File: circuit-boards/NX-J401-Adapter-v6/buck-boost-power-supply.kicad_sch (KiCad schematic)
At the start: 55 parts, among them Q3 CSD19534Q5A, Q4 CSD17578Q5A, Q6 CSD19534Q5A, Q7 CSD17578Q5A

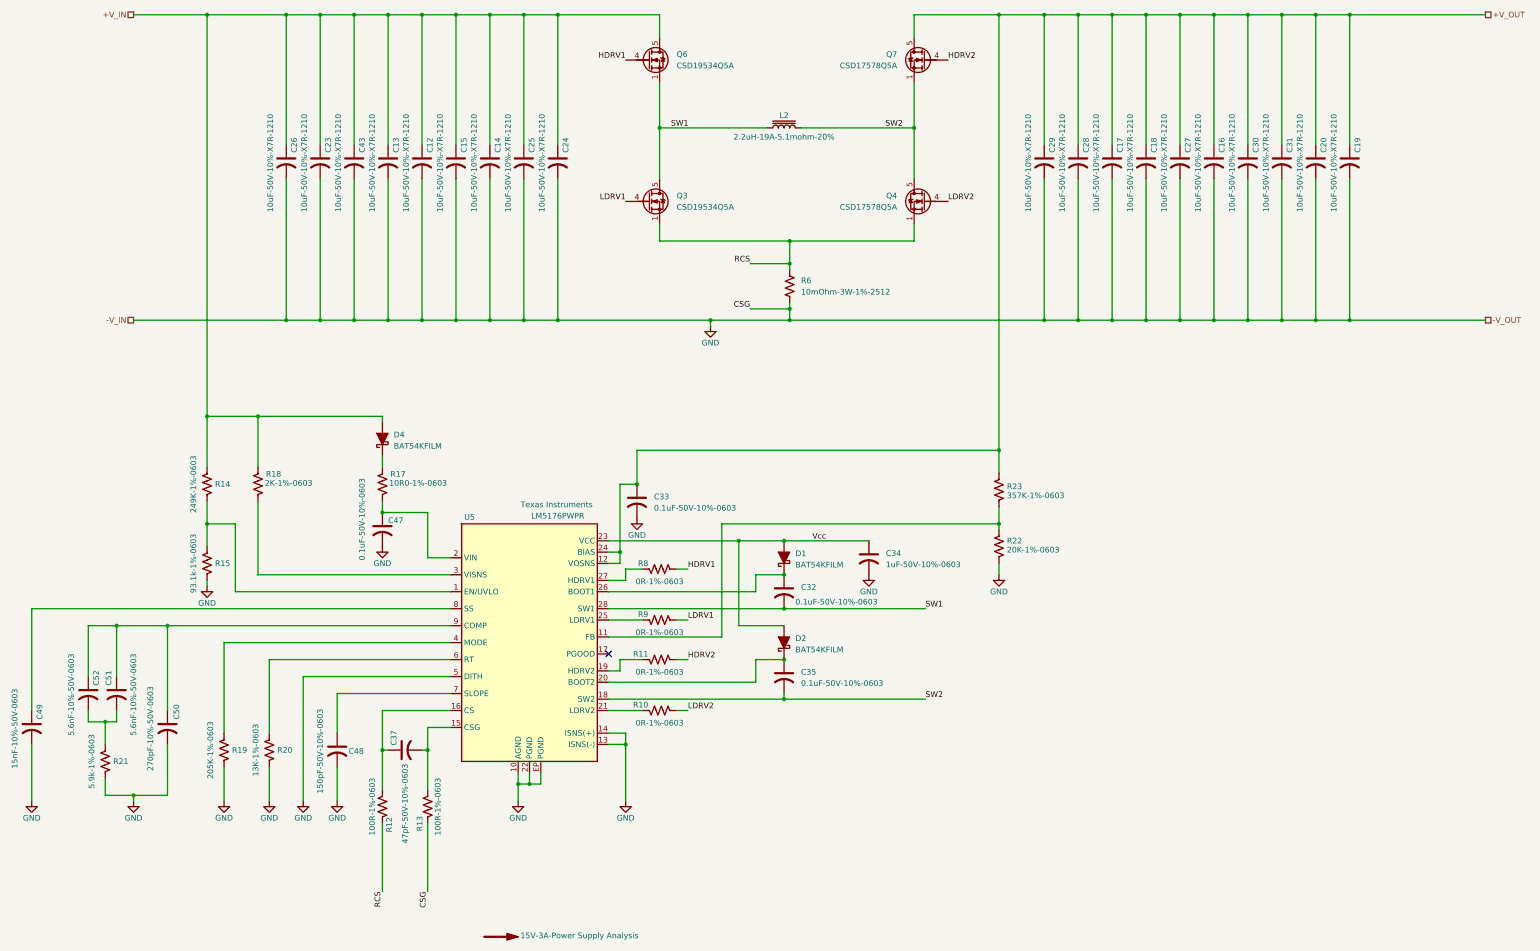
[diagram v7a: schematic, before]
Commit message: Adjusted connector positioning to more closely match J401.
Signed-off-by: Scott Berman <sgberman1@gmail.com>
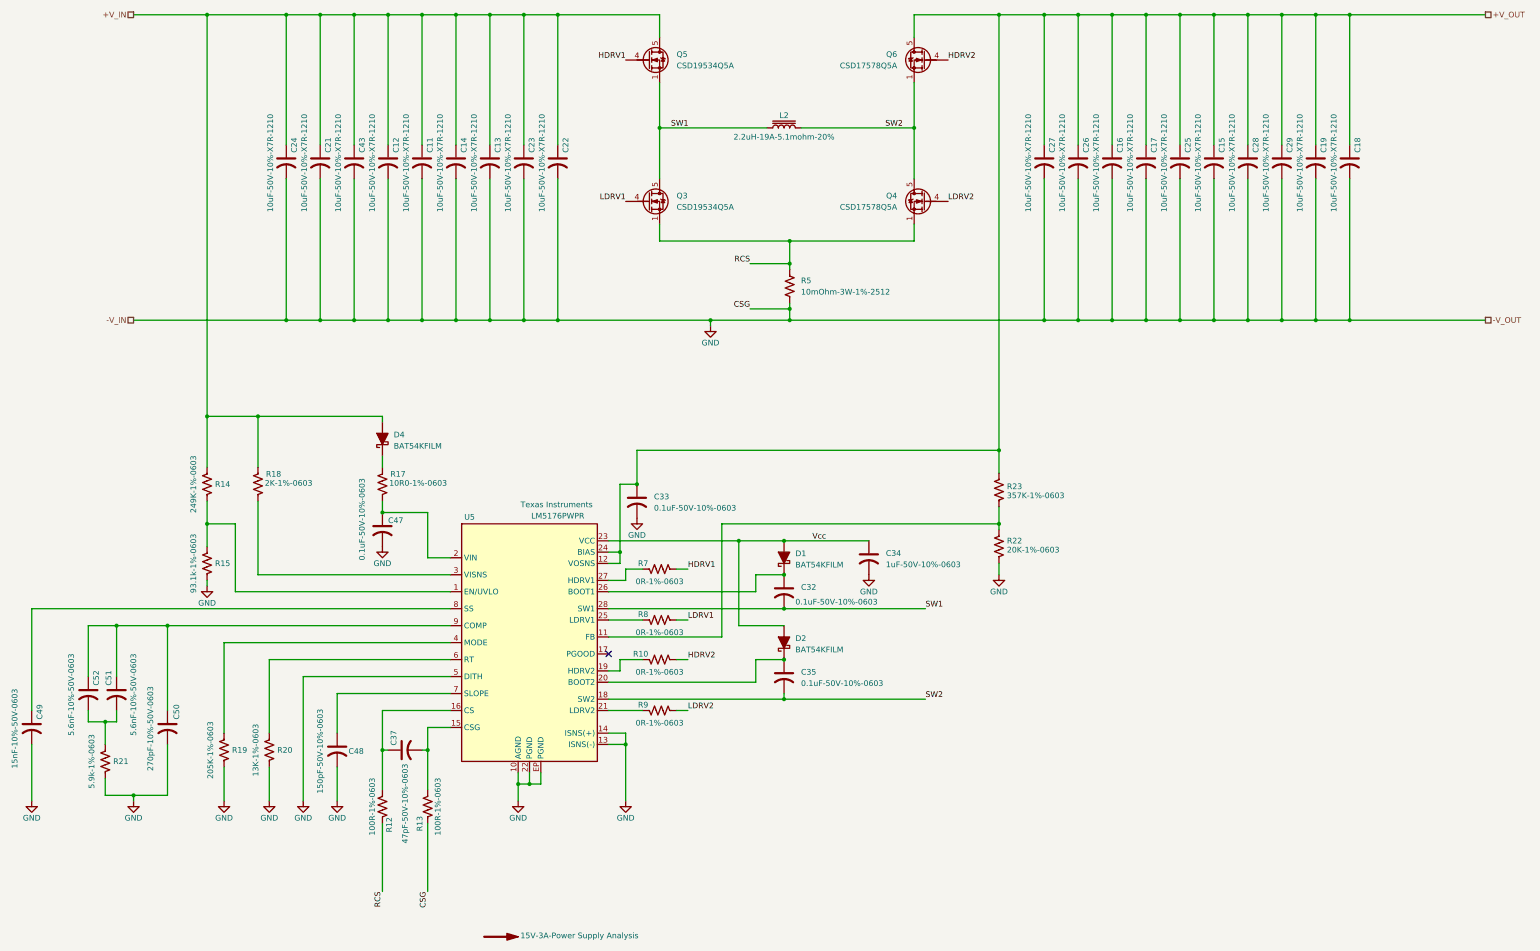
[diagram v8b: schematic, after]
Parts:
- renumbered C12 to C11, C13 to C12, C14 to C13, C15 to C14, C16 to C15, C17 to C16, C18 to C17, C19 to C18, C20 to C19, C23 to C21, C24 to C22, C25 to C23, C26 to C24, C27 to C25, C28 to C26, C29 to C27, C30 to C28, C31 to C29, Q6 to Q5, Q7 to Q6, R11 to R10, R6 to R5, R8 to R7, R9 to R8, R10 to R9
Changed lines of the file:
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@@
 		(dnp no)
 		(fields_autoplaced yes)
-		(property "Reference" "R6"
+		(property "Reference" "R5"
 			(at 205.74 93.9799 0)
 			(show_name no)
@@
 			(project "NX-J401-Adapter-v6"
 				(path "/3c9fa76f-2b37-4666-8575-58caa65def04/048331f9-005d-457c-bfd7-5224f9f99d07"
-					(reference "R6")
+					(reference "R5")
 					(unit 1)
 				)
@@
 		(in_pos_files yes)
 		(dnp no)
-		(property "Reference" "R9"
+		(property "Reference" "R8"
 			(at 171.45 168.91 90)
 			(show_name no)
@@
 			(project "NX-J401-Adapter-v6"
 				(path "/3c9fa76f-2b37-4666-8575-58caa65def04/048331f9-005d-457c-bfd7-5224f9f99d07"
-					(reference "R9")
+					(reference "R8")
 					(unit 1)
 				)
@@
 		(in_pos_files yes)
 		(dnp no)
-		(property "Reference" "C31"
+		(property "Reference" "C29"
 			(at 315.468 65.278 90)
 			(show_name no)
@@
 			(project "NX-J401-Adapter-v6"
 				(path "/3c9fa76f-2b37-4666-8575-58caa65def04/048331f9-005d-457c-bfd7-5224f9f99d07"
-					(reference "C31")
+					(reference "C29")
 					(unit 1)
 				)
@@
 		(in_pos_files yes)
 		(dnp no)
-		(property "Reference" "C23"
+		(property "Reference" "C21"
 			(at 99.568 65.278 90)
 			(show_name no)
@@
 			(project "NX-J401-Adapter-v6"
 				(path "/3c9fa76f-2b37-4666-8575-58caa65def04/048331f9-005d-457c-bfd7-5224f9f99d07"
-					(reference "C23")
+					(reference "C21")
 					(unit 1)
 				)
@@
 		(in_pos_files yes)
 		(dnp no)
-		(property "Reference" "C14"
+		(property "Reference" "C13"
 			(at 137.668 65.278 90)
 			(show_name no)
@@
 			(project "NX-J401-Adapter-v6"
 				(path "/3c9fa76f-2b37-4666-8575-58caa65def04/048331f9-005d-457c-bfd7-5224f9f99d07"
-					(reference "C14")
+					(reference "C13")
 					(unit 1)
 				)
@@
 		(in_pos_files yes)
 		(dnp no)
-		(property "Reference" "C12"
+		(property "Reference" "C11"
 			(at 122.428 65.278 90)
 			(show_name no)
@@
 			(project "NX-J401-Adapter-v6"
 				(path "/3c9fa76f-2b37-4666-8575-58caa65def04/048331f9-005d-457c-bfd7-5224f9f99d07"
-					(reference "C12")
+					(reference "C11")
 					(unit 1)
 				)
@@
 		(in_pos_files yes)
 		(dnp no)
-		(property "Reference" "C17"
+		(property "Reference" "C16"
 			(at 277.368 65.278 90)
 			(show_name no)
@@
 			(project "NX-J401-Adapter-v6"
 				(path "/3c9fa76f-2b37-4666-8575-58caa65def04/048331f9-005d-457c-bfd7-5224f9f99d07"
-					(reference "C17")
+					(reference "C16")
 					(unit 1)
 				)
@@
 		(in_pos_files yes)
 		(dnp no)
-		(property "Reference" "Q7"
+		(property "Reference" "Q6"
 			(at 227.33 43.1799 0)
 			(show_name no)
@@
 			(project "NX-J401-Adapter-v6"
 				(path "/3c9fa76f-2b37-4666-8575-58caa65def04/048331f9-005d-457c-bfd7-5224f9f99d07"
-					(reference "Q7")
+					(reference "Q6")
 					(unit 1)
 				)
@@
 		(in_pos_files yes)
 		(dnp no)
-		(property "Reference" "C26"
+		(property "Reference" "C24"
 			(at 91.948 65.278 90)
 			(show_name no)
@@
 			(project "NX-J401-Adapter-v6"
 				(path "/3c9fa76f-2b37-4666-8575-58caa65def04/048331f9-005d-457c-bfd7-5224f9f99d07"
-					(reference "C26")
+					(reference "C24")
 					(unit 1)
 				)
@@
 		(in_pos_files yes)
 		(dnp no)
-		(property "Reference" "C28"
+		(property "Reference" "C26"
 			(at 269.748 65.278 90)
 			(show_name no)
@@
 			(project "NX-J401-Adapter-v6"
 				(path "/3c9fa76f-2b37-4666-8575-58caa65def04/048331f9-005d-457c-bfd7-5224f9f99d07"
-					(reference "C28")
+					(reference "C26")
 					(unit 1)
 				)
@@
 		(in_pos_files yes)
 		(dnp no)
-		(property "Reference" "C27"
+		(property "Reference" "C25"
 			(at 292.608 65.278 90)
 			(show_name no)
@@
 			(project "NX-J401-Adapter-v6"
 				(path "/3c9fa76f-2b37-4666-8575-58caa65def04/048331f9-005d-457c-bfd7-5224f9f99d07"
-					(reference "C27")
+					(reference "C25")
 					(unit 1)
 				)
@@
 		(in_pos_files yes)
 		(dnp no)
-		(property "Reference" "C16"
+		(property "Reference" "C15"
 			(at 300.228 65.278 90)
 			(show_name no)
@@
 			(project "NX-J401-Adapter-v6"
 				(path "/3c9fa76f-2b37-4666-8575-58caa65def04/048331f9-005d-457c-bfd7-5224f9f99d07"
-					(reference "C16")
+					(reference "C15")
 					(unit 1)
 				)
@@
 		(in_pos_files yes)
 		(dnp no)
-		(property "Reference" "C15"
+		(property "Reference" "C14"
 			(at 130.048 65.278 90)
 			(show_name no)
@@
 			(project "NX-J401-Adapter-v6"
 				(path "/3c9fa76f-2b37-4666-8575-58caa65def04/048331f9-005d-457c-bfd7-5224f9f99d07"
-					(reference "C15")
+					(reference "C14")
 					(unit 1)
 				)
@@
 		(in_pos_files yes)
 		(dnp no)
-		(property "Reference" "R11"
+		(property "Reference" "R10"
 			(at 171.45 177.8 90)
 			(show_name no)
@@
 			(project "NX-J401-Adapter-v6"
 				(path "/3c9fa76f-2b37-4666-8575-58caa65def04/048331f9-005d-457c-bfd7-5224f9f99d07"
-					(reference "R11")
+					(reference "R10")
 					(unit 1)
 				)
@@
 		(in_pos_files yes)
 		(dnp no)
-		(property "Reference" "R10"
+		(property "Reference" "R9"
 			(at 171.45 189.23 90)
 			(show_name no)
@@
 			(project "NX-J401-Adapter-v6"
 				(path "/3c9fa76f-2b37-4666-8575-58caa65def04/048331f9-005d-457c-bfd7-5224f9f99d07"
-					(reference "R10")
+					(reference "R9")
 					(unit 1)
 				)
@@
 		(in_pos_files yes)
 		(dnp no)
-		(property "Reference" "C25"
+		(property "Reference" "C23"
 			(at 145.288 65.278 90)
 			(show_name no)
@@
 			(project "NX-J401-Adapter-v6"
 				(path "/3c9fa76f-2b37-4666-8575-58caa65def04/048331f9-005d-457c-bfd7-5224f9f99d07"
-					(reference "C25")
+					(reference "C23")
 					(unit 1)
 				)
@@
 		(in_pos_files yes)
 		(dnp no)
-		(property "Reference" "C29"
+		(property "Reference" "C27"
 			(at 262.128 65.278 90)
 			(show_name no)
@@
 			(project "NX-J401-Adapter-v6"
 				(path "/3c9fa76f-2b37-4666-8575-58caa65def04/048331f9-005d-457c-bfd7-5224f9f99d07"
-					(reference "C29")
+					(reference "C27")
 					(unit 1)
 				)
@@
 		(in_pos_files yes)
 		(dnp no)
-		(property "Reference" "C30"
+		(property "Reference" "C28"
 			(at 307.848 65.278 90)
 			(show_name no)
@@
 			(project "NX-J401-Adapter-v6"
 				(path "/3c9fa76f-2b37-4666-8575-58caa65def04/048331f9-005d-457c-bfd7-5224f9f99d07"
-					(reference "C30")
+					(reference "C28")
 					(unit 1)
 				)
@@
 		(in_pos_files yes)
 		(dnp no)
-		(property "Reference" "R8"
+		(property "Reference" "R7"
 			(at 171.45 157.48 90)
 			(show_name no)
@@
 			(project "NX-J401-Adapter-v6"
 				(path "/3c9fa76f-2b37-4666-8575-58caa65def04/048331f9-005d-457c-bfd7-5224f9f99d07"
-					(reference "R8")
+					(reference "R7")
 					(unit 1)
 				)
@@
 		(in_pos_files yes)
 		(dnp no)
-		(property "Reference" "C24"
+		(property "Reference" "C22"
 			(at 152.908 65.278 90)
 			(show_name no)
@@
 			(project "NX-J401-Adapter-v6"
 				(path "/3c9fa76f-2b37-4666-8575-58caa65def04/048331f9-005d-457c-bfd7-5224f9f99d07"
-					(reference "C24")
+					(reference "C22")
 					(unit 1)
 				)
@@
 		(dnp no)
 		(fields_autoplaced yes)
-		(property "Reference" "Q6"
+		(property "Reference" "Q5"
 			(at 177.8 43.1799 0)
 			(show_name no)
@@
 			(project "NX-J401-Adapter-v6"
 				(path "/3c9fa76f-2b37-4666-8575-58caa65def04/048331f9-005d-457c-bfd7-5224f9f99d07"
-					(reference "Q6")
+					(reference "Q5")
 					(unit 1)
 				)
@@
 		(in_pos_files yes)
 		(dnp no)
-		(property "Reference" "C18"
+		(property "Reference" "C17"
 			(at 284.988 65.278 90)
 			(show_name no)
@@
 			(project "NX-J401-Adapter-v6"
 				(path "/3c9fa76f-2b37-4666-8575-58caa65def04/048331f9-005d-457c-bfd7-5224f9f99d07"
-					(reference "C18")
+					(reference "C17")
 					(unit 1)
 				)
@@
 		(in_pos_files yes)
 		(dnp no)
-		(property "Reference" "C19"
+		(property "Reference" "C18"
 			(at 330.708 65.278 90)
 			(show_name no)
@@
 			(project "NX-J401-Adapter-v6"
 				(path "/3c9fa76f-2b37-4666-8575-58caa65def04/048331f9-005d-457c-bfd7-5224f9f99d07"
-					(reference "C19")
+					(reference "C18")
 					(unit 1)
 				)
@@
 		(in_pos_files yes)
 		(dnp no)
-		(property "Reference" "C13"
+		(property "Reference" "C12"
 			(at 114.808 65.278 90)
 			(show_name no)
@@
 			(project "NX-J401-Adapter-v6"
 				(path "/3c9fa76f-2b37-4666-8575-58caa65def04/048331f9-005d-457c-bfd7-5224f9f99d07"
-					(reference "C13")
+					(reference "C12")
 					(unit 1)
 				)
@@
 		(in_pos_files yes)
 		(dnp no)
-		(property "Reference" "C20"
+		(property "Reference" "C19"
 			(at 323.088 65.278 90)
 			(show_name no)
@@
 			(project "NX-J401-Adapter-v6"
 				(path "/3c9fa76f-2b37-4666-8575-58caa65def04/048331f9-005d-457c-bfd7-5224f9f99d07"
-					(reference "C20")
+					(reference "C19")
 					(unit 1)
 				)
